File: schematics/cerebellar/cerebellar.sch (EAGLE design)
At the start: 67 parts, among them CON2 ODrive1, CON4 Odrive3, CON5 ODrive4, CON6 Odrive2, CON7 ODrive5, CON8 ODrive6, IC3 LTC7001, P1 Foot1, P10 SPI2, P11 Foot2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

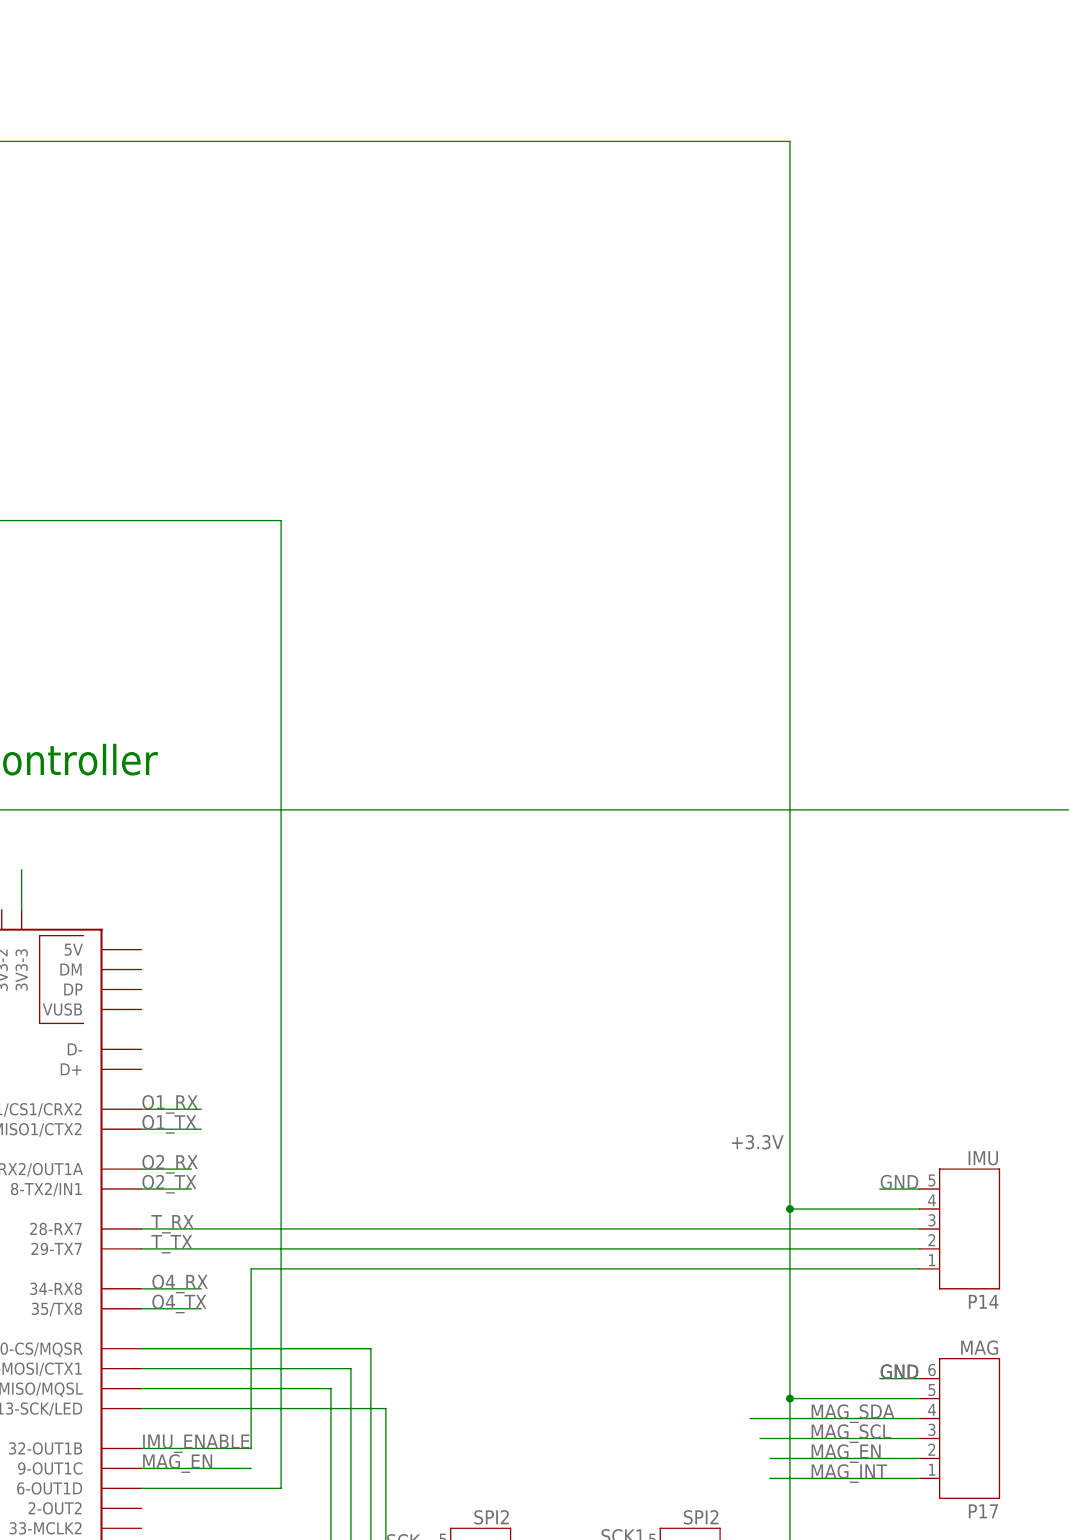
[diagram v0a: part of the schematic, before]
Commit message: fixed socket of IMU layout
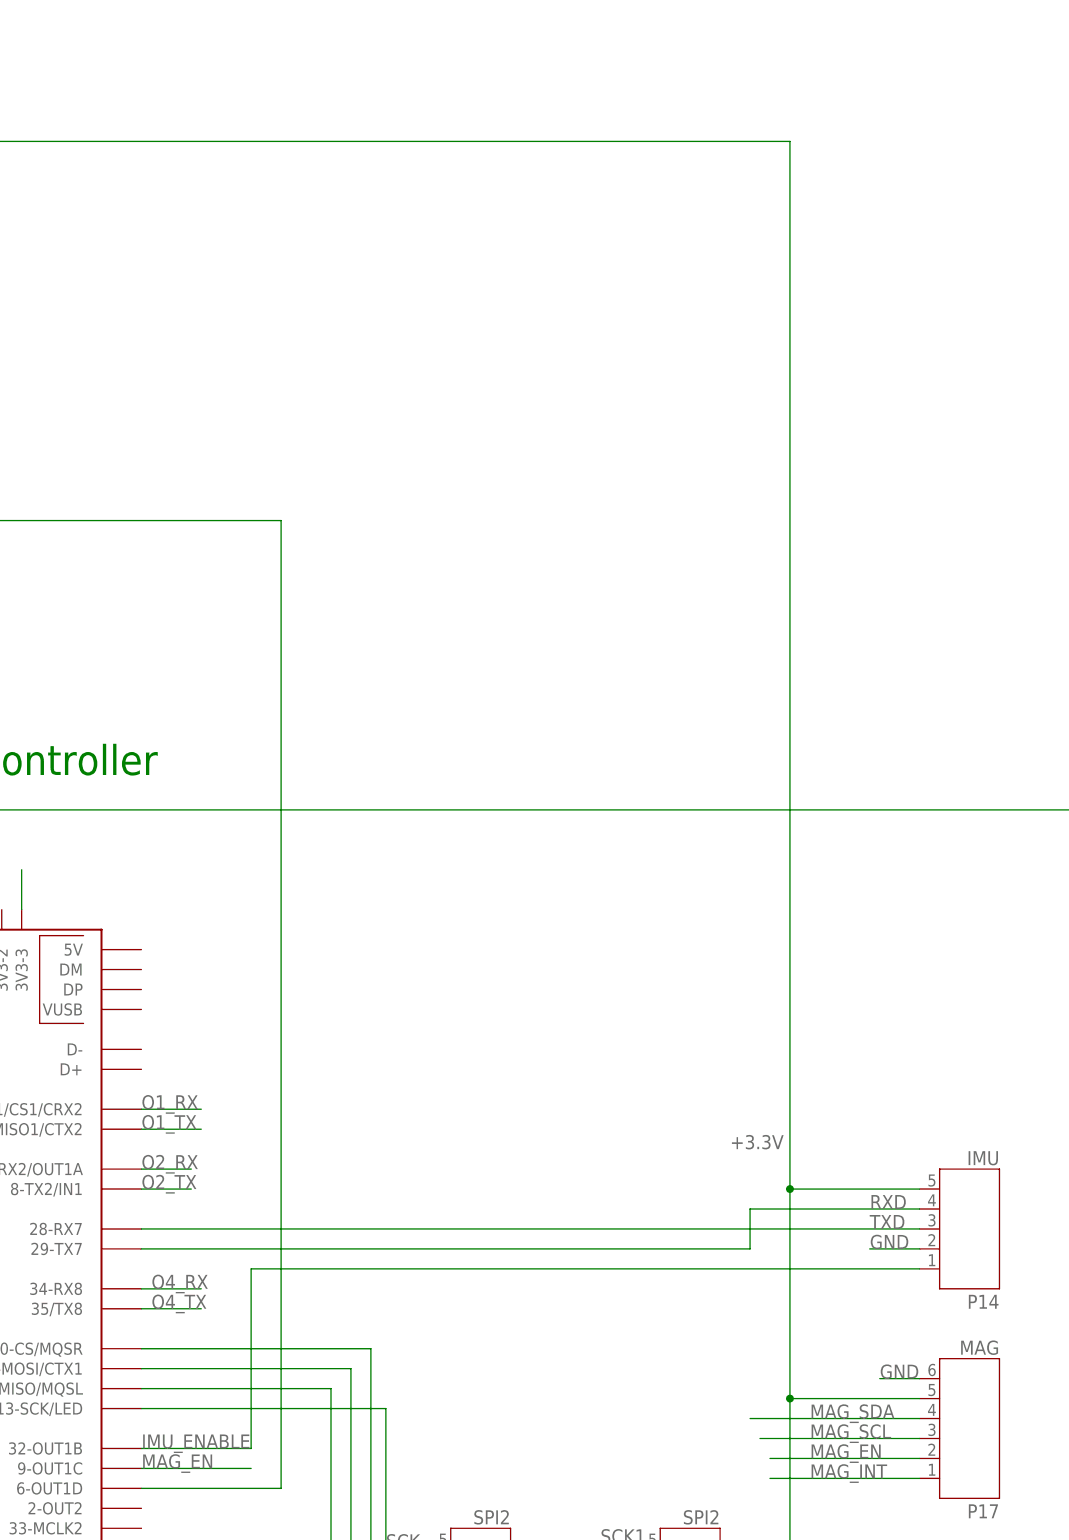
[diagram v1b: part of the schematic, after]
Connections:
- net T_RX renamed TXD
- removed net T_TX: P14.2, U$1.29-TX7
- new net RXD: P14.4, U$1.29-TX7
- net +3.3V: now also P14.5; no longer P14.4
- net GND: now also P14.2; no longer P14.5
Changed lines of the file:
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@@
-</segment>
-<segment>
-<pinref part="P14" gate="G$1" pin="5"/>
-<wire x1="248.92" y1="44.45" x2="243.84" y2="44.45" width="0.1524" layer="91"/>
-<label x="243.84" y="44.45" size="1.778" layer="95"/>
-<label x="243.84" y="20.32" size="1.778" layer="95"/>
 </segment>
 <segment>
@@
 <pinref part="P17" gate="A" pin="6"/>
 </segment>
-</net>
-<net name="T_TX" class="0">
-<segment>
-<pinref part="U$1" gate="G$1" pin="29-TX7"/>
-<label x="151.13" y="36.83" size="1.778" layer="95"/>
+<segment>
 <pinref part="P14" gate="G$1" pin="2"/>
-<wire x1="149.86" y1="36.83" x2="248.92" y2="36.83" width="0.1524" layer="91"/>
-</segment>
-</net>
-<net name="T_RX" class="0">
-<segment>
-<pinref part="U$1" gate="G$1" pin="28-RX7"/>
-<label x="151.13" y="39.37" size="1.778" layer="95"/>
-<pinref part="P14" gate="G$1" pin="3"/>
-<wire x1="149.86" y1="39.37" x2="248.92" y2="39.37" width="0.1524" layer="91"/>
+<wire x1="248.92" y1="36.83" x2="242.57" y2="36.83" width="0.1524" layer="91"/>
+<label x="242.57" y="36.83" size="1.778" layer="95"/>
 </segment>
 </net>
@@
 <net name="+3.3V" class="0">
 <segment>
-<pinref part="P14" gate="G$1" pin="4"/>
-<wire x1="232.41" y1="41.91" x2="248.92" y2="41.91" width="0.1524" layer="91"/>
 <wire x1="248.92" y1="17.78" x2="232.41" y2="17.78" width="0.1524" layer="91"/>
-<wire x1="232.41" y1="17.78" x2="232.41" y2="41.91" width="0.1524" layer="91"/>
 <pinref part="P17" gate="A" pin="5"/>
-<junction x="232.41" y="41.91"/>
 <label x="224.79" y="49.53" size="1.778" layer="95"/>
 <pinref part="U$6" gate="G$1" pin="OUT"/>
@@
 <junction x="238.76" y="-91.44"/>
 <pinref part="C4" gate="G$1" pin="1"/>
-<wire x1="232.41" y1="41.91" x2="232.41" y2="177.8" width="0.1524" layer="91"/>
+<wire x1="232.41" y1="17.78" x2="232.41" y2="44.45" width="0.1524" layer="91"/>
+<wire x1="232.41" y1="44.45" x2="232.41" y2="177.8" width="0.1524" layer="91"/>
 <wire x1="232.41" y1="17.78" x2="232.41" y2="-91.44" width="0.1524" layer="91"/>
 <wire x1="232.41" y1="-91.44" x2="238.76" y2="-91.44" width="0.1524" layer="91"/>
 <junction x="232.41" y="17.78"/>
+<pinref part="P14" gate="G$1" pin="5"/>
+<wire x1="248.92" y1="44.45" x2="232.41" y2="44.45" width="0.1524" layer="91"/>
+<junction x="232.41" y="44.45"/>
 </segment>
 </net>
@@
 </segment>
 </net>
+<net name="TXD" class="0">
+<segment>
+<pinref part="U$1" gate="G$1" pin="28-RX7"/>
+<wire x1="149.86" y1="39.37" x2="248.92" y2="39.37" width="0.1524" layer="91"/>
+<pinref part="P14" gate="G$1" pin="3"/>
+<label x="242.57" y="39.37" size="1.778" layer="95"/>
+</segment>
+</net>
+<net name="RXD" class="0">
+<segment>
+<pinref part="U$1" gate="G$1" pin="29-TX7"/>
+<wire x1="149.86" y1="36.83" x2="227.33" y2="36.83" width="0.1524" layer="91"/>
+<wire x1="227.33" y1="36.83" x2="227.33" y2="41.91" width="0.1524" layer="91"/>
+<pinref part="P14" gate="G$1" pin="4"/>
+<wire x1="227.33" y1="41.91" x2="248.92" y2="41.91" width="0.1524" layer="91"/>
+<label x="242.57" y="41.91" size="1.778" layer="95"/>
+</segment>
+</net>
